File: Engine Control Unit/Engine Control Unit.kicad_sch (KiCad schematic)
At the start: 9 parts, among them J3 Conn_01x02_Socket

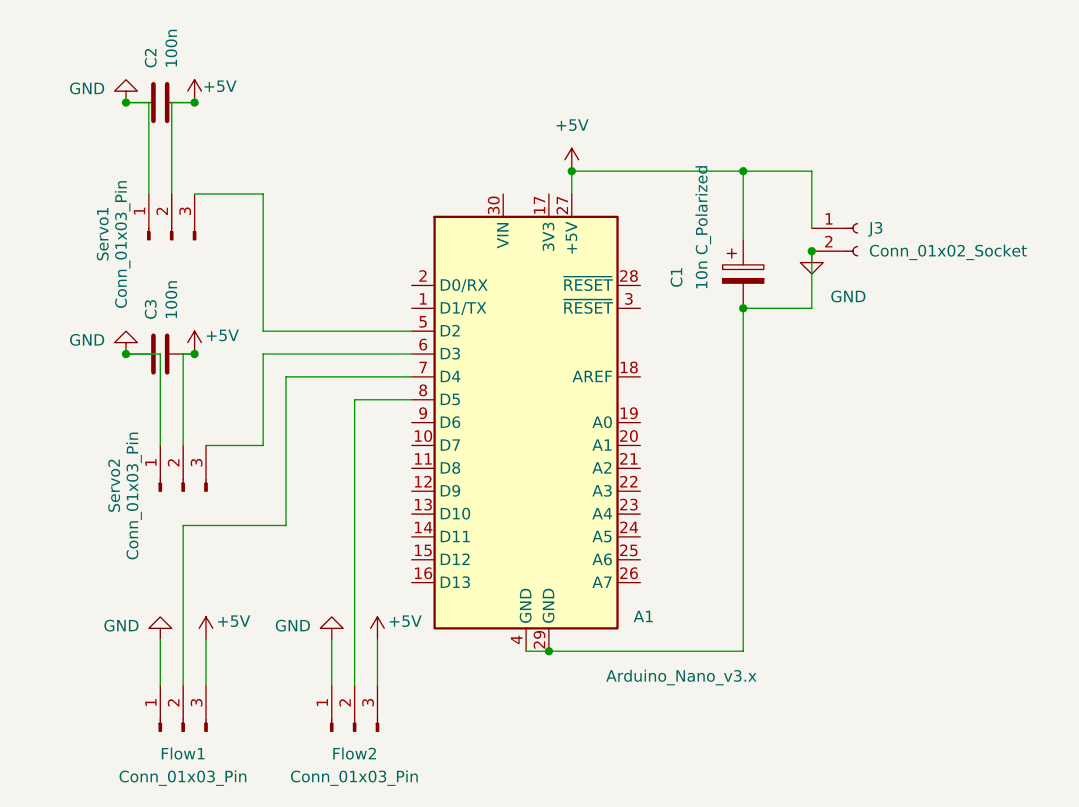
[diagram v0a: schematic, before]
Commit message: :bug: (Pins) Change pins to interupt
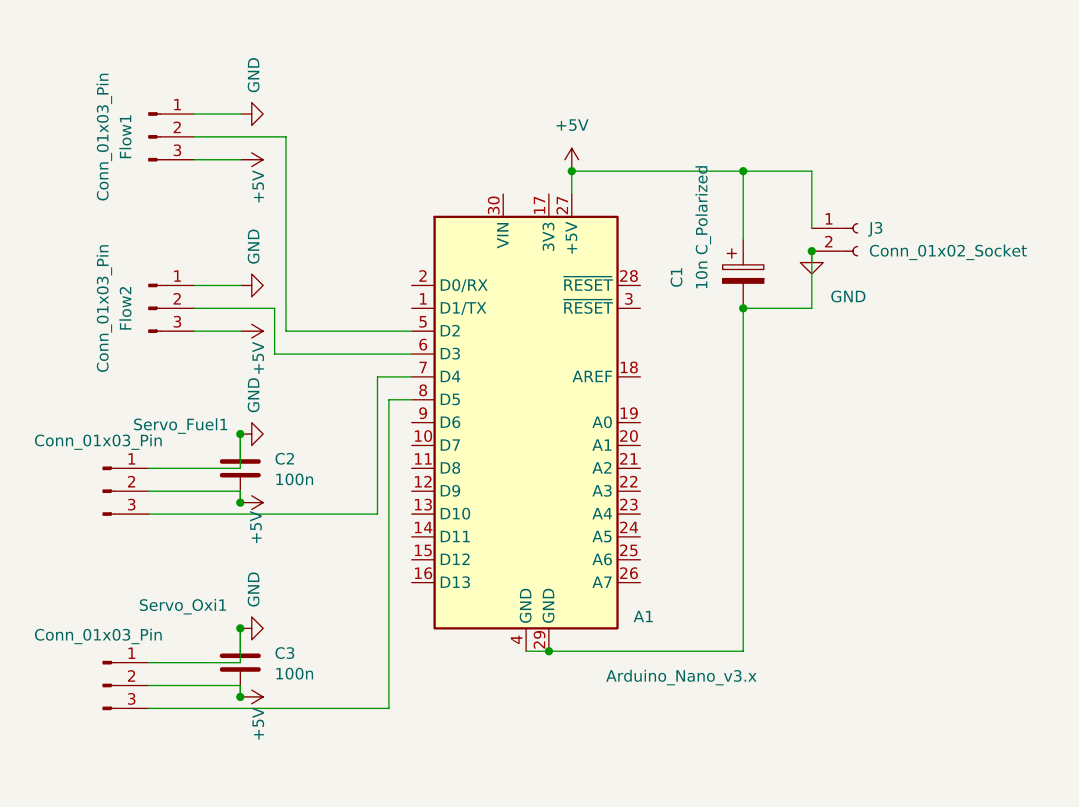
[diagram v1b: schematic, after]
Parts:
- renumbered Servo1 to Servo_Fuel1, Servo2 to Servo_Oxi1
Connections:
- net at Servo_Oxi1.3 (Pin_3): now also A1.8 (D5); no longer A1.6 (D3)
- net at Servo_Fuel1.3 (Pin_3): now also A1.7 (D4); no longer A1.5 (D2)
- net at Flow2.2 (Pin_2): now also A1.6 (D3); no longer A1.8 (D5)
- net at Flow1.2 (Pin_2): now also A1.5 (D2); no longer A1.7 (D4)
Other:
- moved on the sheet: C2, C3, Flow1, Flow2, Servo_Fuel1, Servo_Oxi1
